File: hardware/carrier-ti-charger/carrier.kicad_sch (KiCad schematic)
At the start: 0 parts

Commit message: TI charger
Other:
- sheet Charger MAX77757 renamed Charger BQ25798
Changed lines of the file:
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@@
 			(color 0 0 0 0)
 		)
-		(property "Sheetname" "Charger MAX77757"
+		(property "Sheetname" "Charger BQ25798"
 			(at 73.66 50.04 0)
 			(show_name no)

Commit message: Switch parts (BMP580, TPS259474L) due to stock shortage.
Also, add overvoltage (OVLO) protection.
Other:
- note added: "Piezo, Schmitt driver, mute switch BMP580 barometer on I2C"
- note removed: "Piezo, Schmitt driver, mute switch BMP581 barometer on I2C"
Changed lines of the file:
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@@
 		)
 	)
-	(text "Piezo, Schmitt driver, mute switch\nBMP581 barometer on I2C"
+	(text "Piezo, Schmitt driver, mute switch\nBMP580 barometer on I2C"
 		(exclude_from_sim no)
 		(at 234.95 109.22 0)

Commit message: Other MH's.
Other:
- note added: "+5V 5 V"
- note added: "+ESP_3V3, I2C, BUZZ_PWM"
- note added: "+VBAT, +VSYS"
- note added: "+VBAT, charger status"
- note added: "+VSYS, PWR_EN"
- note added: "+VUSB 5 V"
- note removed: "ESP_3V3, I2C, BUZZ_PWM"
- note removed: "RAIL_5V 5 V"
- note removed: "USB_VBUS 5 V"
- note removed: "VBAT, VSYS"
- note removed: "VBAT, charger status"
- note removed: "VSYS, PWR_EN"
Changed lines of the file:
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@@
 		)
 	)
-	(text "VBAT, VSYS"
+	(text "+VBAT, +VSYS"
 		(exclude_from_sim no)
 		(at 119.38 65.04 0)
@@
 		)
 	)
-	(text "ESP_3V3, I2C, BUZZ_PWM"
+	(text "+ESP_3V3, I2C, BUZZ_PWM"
 		(exclude_from_sim no)
 		(at 268.2 94.48 0)
@@
 		)
 	)
-	(text "VBAT, charger status"
+	(text "+VBAT, charger status"
 		(exclude_from_sim no)
 		(at 161.52 94.48 0)
@@
 		)
 	)
-	(text "USB_VBUS 5 V"
+	(text "+VUSB 5 V"
 		(exclude_from_sim no)
 		(at 66.04 65.04 0)
@@
 		)
 	)
-	(text "RAIL_5V 5 V"
+	(text "+5V 5 V"
 		(exclude_from_sim no)
 		(at 226.06 65.04 0)
@@
 		)
 	)
-	(text "VSYS, PWR_EN"
+	(text "+VSYS, PWR_EN"
 		(exclude_from_sim no)
 		(at 172.72 65.04 0)
@@
 		(stroke
 			(width 0.254)
-			(type default)
+			(type solid)
+			(color 255 14 25 1)
 		)
 	)
@@
 		(stroke
 			(width 0.254)
-			(type default)
+			(type solid)
+			(color 255 14 25 1)
 		)
 	)
@@
 		(stroke
 			(width 0.254)
-			(type default)
+			(type solid)
+			(color 255 14 25 1)
 		)
 	)
@@
 		(stroke
 			(width 0.254)
-			(type default)
+			(type solid)
+			(color 255 14 25 1)
 		)
 	)
@@
 		(stroke
 			(width 0.254)
-			(type default)
-		)
-	)
+			(type solid)
+			(color 255 14 25 1)
+		)
+	)

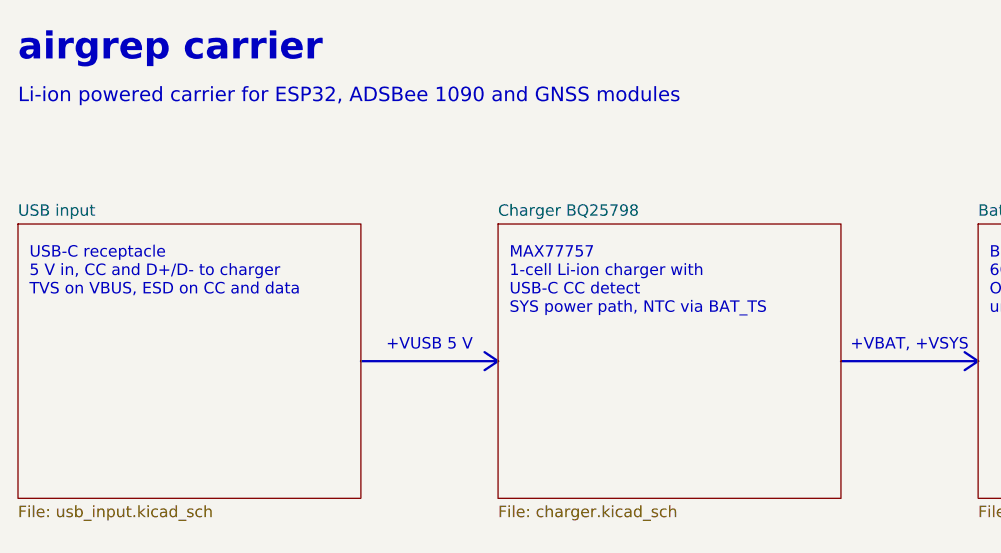
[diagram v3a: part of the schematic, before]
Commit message: Add USB current detection.
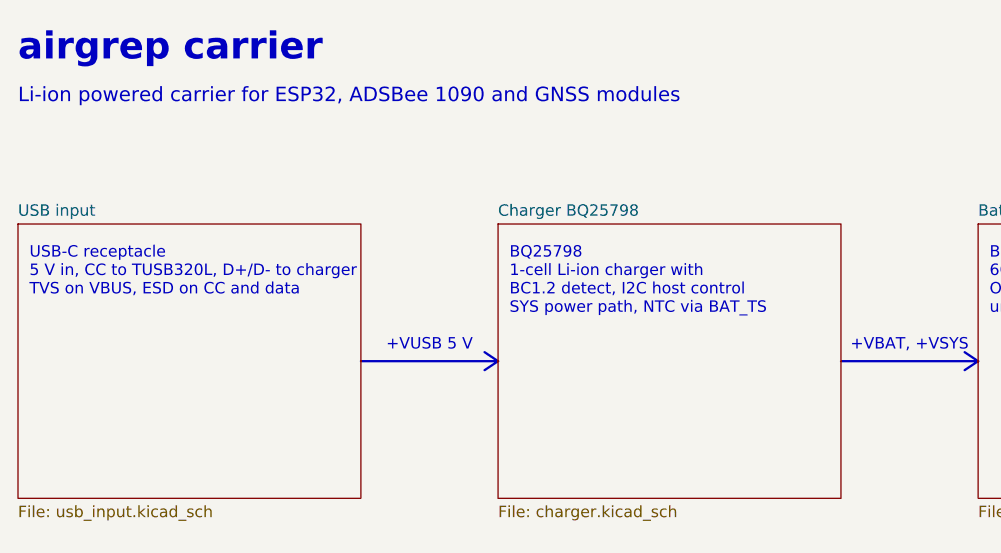
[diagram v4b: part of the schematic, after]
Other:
- note added: "BQ25798 1-cell Li-ion charger with BC1.2 detect, I2C host control SYS power path, NTC via BAT_TS"
- note added: "USB-C receptacle 5 V in, CC to TUSB320L, D+/D- to charger TVS on VBUS, ESD on CC and data"
- note removed: "MAX77757 1-cell Li-ion charger with USB-C CC detect SYS power path, NTC via BAT_TS"
- note removed: "USB-C receptacle 5 V in, CC and D+/D- to charger TVS on VBUS, ESD on CC and data"
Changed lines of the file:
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@@
 		)
 	)
-	(text "MAX77757\n1-cell Li-ion charger with\nUSB-C CC detect\nSYS power path, NTC via BAT_TS"
+	(text "BQ25798\n1-cell Li-ion charger with\nBC1.2 detect, I2C host control\nSYS power path, NTC via BAT_TS"
 		(exclude_from_sim no)
 		(at 74.93 53.34 0)
@@
 		)
 	)
-	(text "USB-C receptacle\n5 V in, CC and D+/D- to charger\nTVS on VBUS, ESD on CC and data"
+	(text "USB-C receptacle\n5 V in, CC to TUSB320L, D+/D- to charger\nTVS on VBUS, ESD on CC and data"
 		(exclude_from_sim no)
 		(at 21.59 53.34 0)

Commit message: Switch to faster FUSB303B USB controller.
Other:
- note added: "USB-C receptacle 5 V in, CC to FUSB303B, D+/D- to charger TVS on VBUS, ESD on data"
- note removed: "USB-C receptacle 5 V in, CC to TUSB320L, D+/D- to charger TVS on VBUS, ESD on CC and data"
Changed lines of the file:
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@@
 		)
 	)
-	(text "USB-C receptacle\n5 V in, CC to TUSB320L, D+/D- to charger\nTVS on VBUS, ESD on CC and data"
+	(text "USB-C receptacle\n5 V in, CC to FUSB303B, D+/D- to charger\nTVS on VBUS, ESD on data"
 		(exclude_from_sim no)
 		(at 21.59 53.34 0)

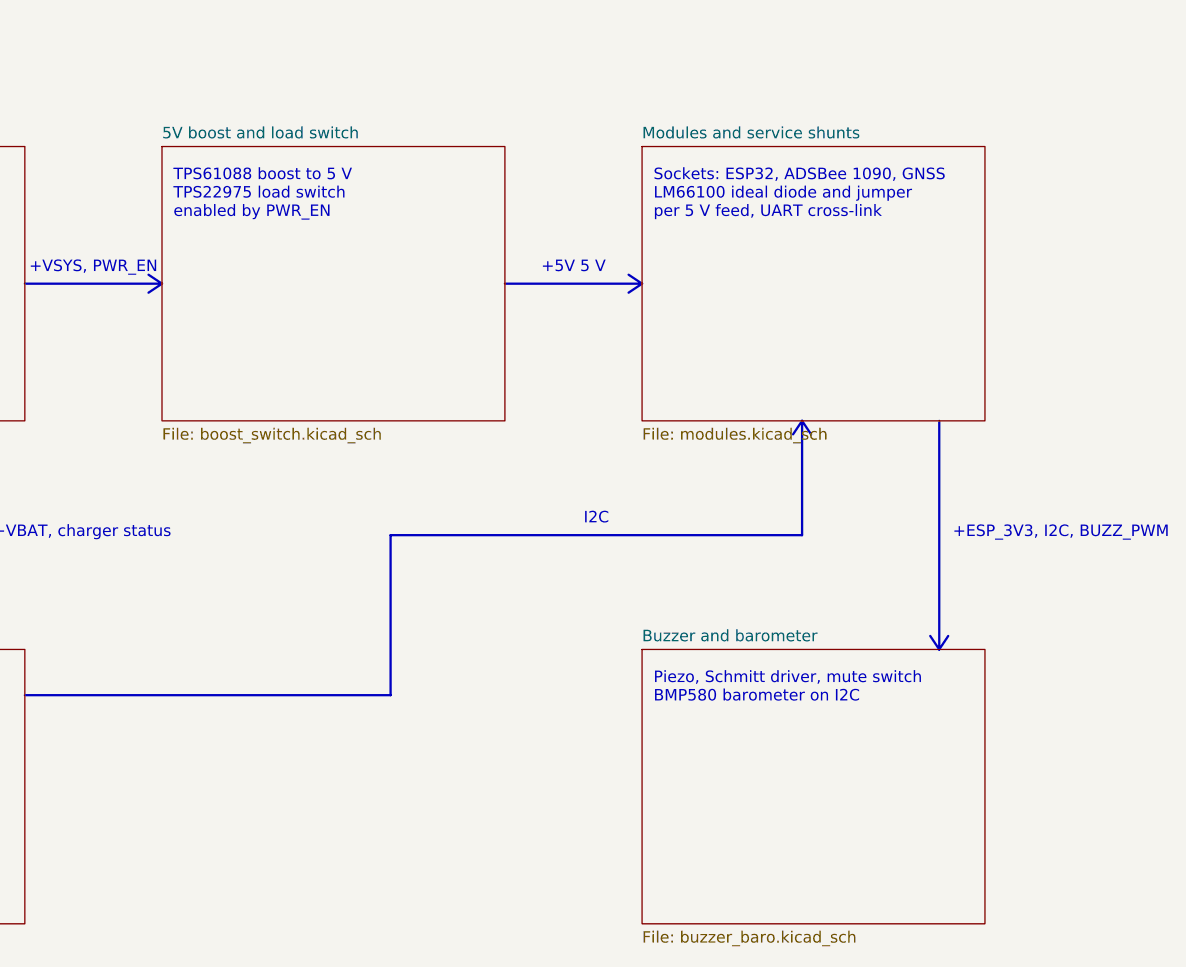
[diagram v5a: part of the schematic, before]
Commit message: Switch to Max M10 on-board chip instead of module.
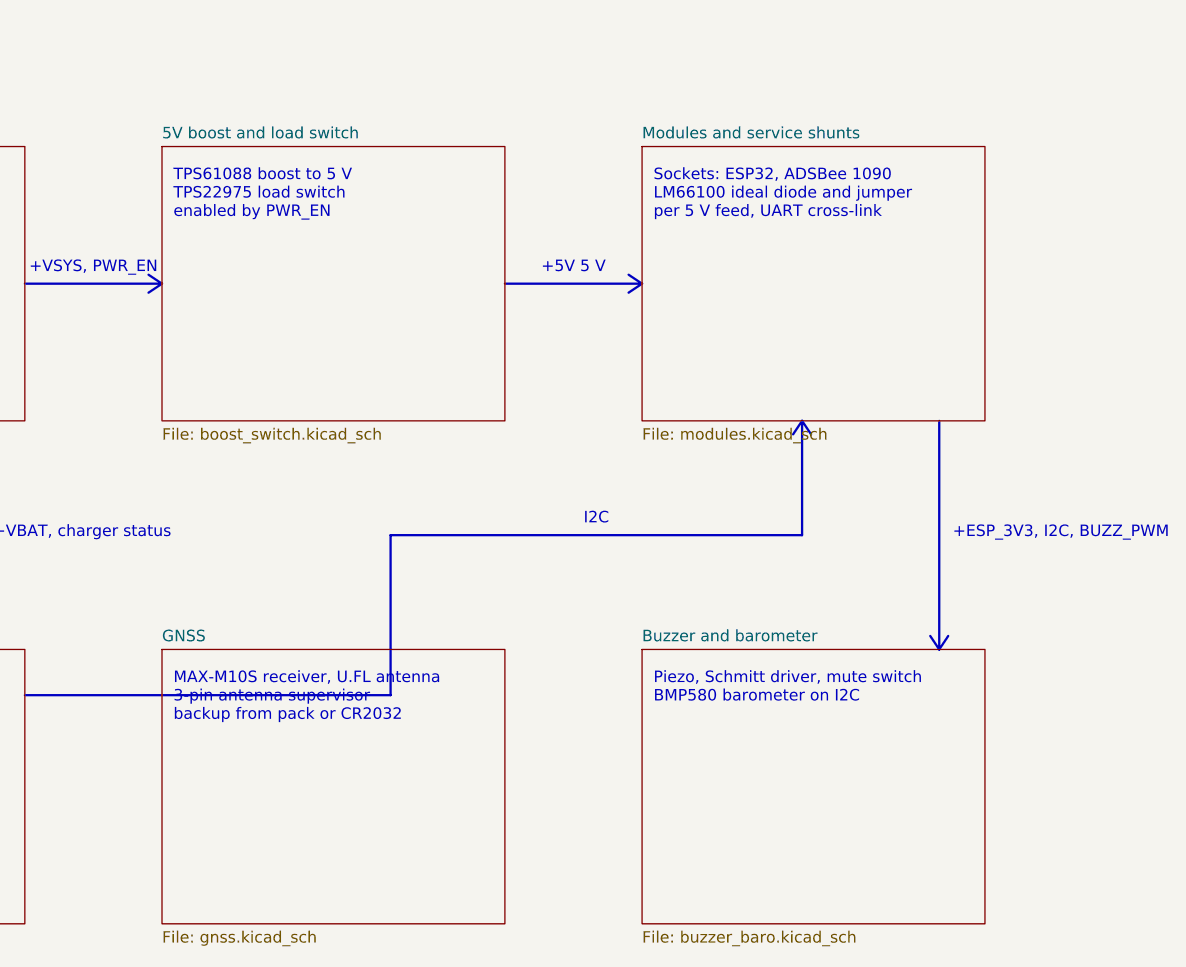
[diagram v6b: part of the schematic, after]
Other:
- added sheet GNSS (gnss.kicad_sch)
- note added: "MAX-M10S receiver, U.FL antenna 3-pin antenna supervisor backup from pack or CR2032"
- note added: "Sockets: ESP32, ADSBee 1090 LM66100 ideal diode and jumper per 5 V feed, UART cross-link"
- note removed: "Sockets: ESP32, ADSBee 1090, GNSS LM66100 ideal diode and jumper per 5 V feed, UART cross-link"
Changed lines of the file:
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@@
 		)
 	)
-	(text "Sockets: ESP32, ADSBee 1090, GNSS\nLM66100 ideal diode and jumper\nper 5 V feed, UART cross-link"
+	(text "Sockets: ESP32, ADSBee 1090\nLM66100 ideal diode and jumper\nper 5 V feed, UART cross-link"
 		(exclude_from_sim no)
 		(at 234.95 53.34 0)
@@
 		)
 	)
+	(sheet
+		(at 180.34 106.68)
+		(size 38.1 30.48)
+		(exclude_from_sim no)
+		(in_bom yes)
+		(on_board yes)
+		(dnp no)
+		(stroke
+			(width 0.0006)
+			(type solid)
+		)
+		(fill
+			(color 0 0 0 0)
+		)
+		(property "Sheetname" "GNSS"
+			(at 180.34 105.92 0)
+			(show_name no)
+			(do_not_autoplace no)
+			(effects
+				(font
+					(size 1.27 1.27)
+				)
+				(justify left bottom)
+			)
+		)
+		(property "Sheetfile" "gnss.kicad_sch"
+			(at 180.34 137.92 0)
+			(show_name no)
+			(do_not_autoplace no)
+			(effects
+				(font
+					(size 1.27 1.27)
+				)
+				(justify left top)
+			)
+		)
+		(instances
+			(project "carrier"
+				(path "/1d76d2ec-7795-4c71-8167-b1182c3ebc1d"
+					(page "9")
+				)
+			)
+		)
+	)
+	(text "MAX-M10S receiver, U.FL antenna\n3-pin antenna supervisor\nbackup from pack or CR2032"
+		(exclude_from_sim no)
+		(at 181.61 109.22 0)
+		(effects
+			(font
+				(size 1.27 1.27)
+			)
+			(justify left top)
+		)
+	)
